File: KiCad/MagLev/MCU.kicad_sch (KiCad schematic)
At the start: 70 parts, among them J2 Programming header, J4 USB_B_Micro, Q1 ZX5T851GTA, Q16 TEMT7000X01, U6 ATmega328P-A, U8 FT232RL, U9 LM1117MP-5.0, Y3 J49SMH-16MHz

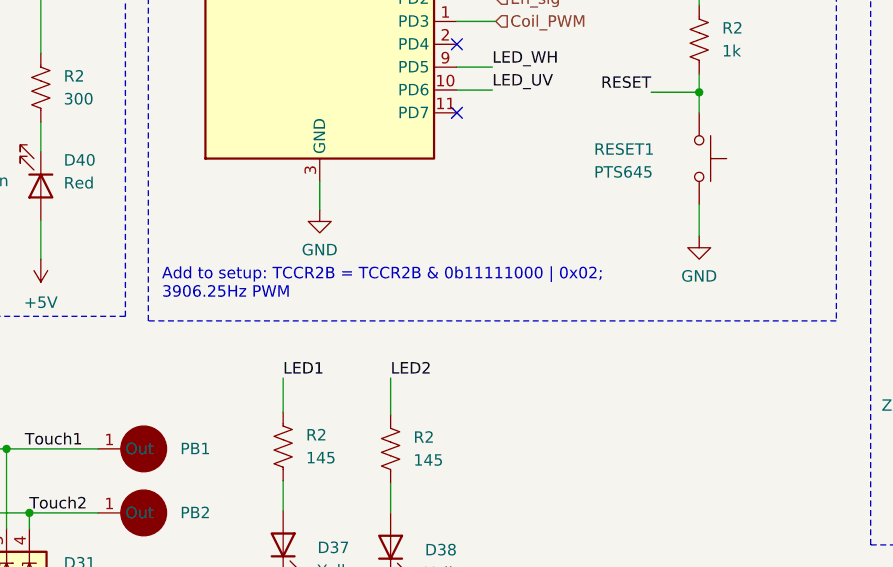
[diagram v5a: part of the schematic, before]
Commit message: Remove silkscreen components from back layer. Cleanup schematic and pcb.
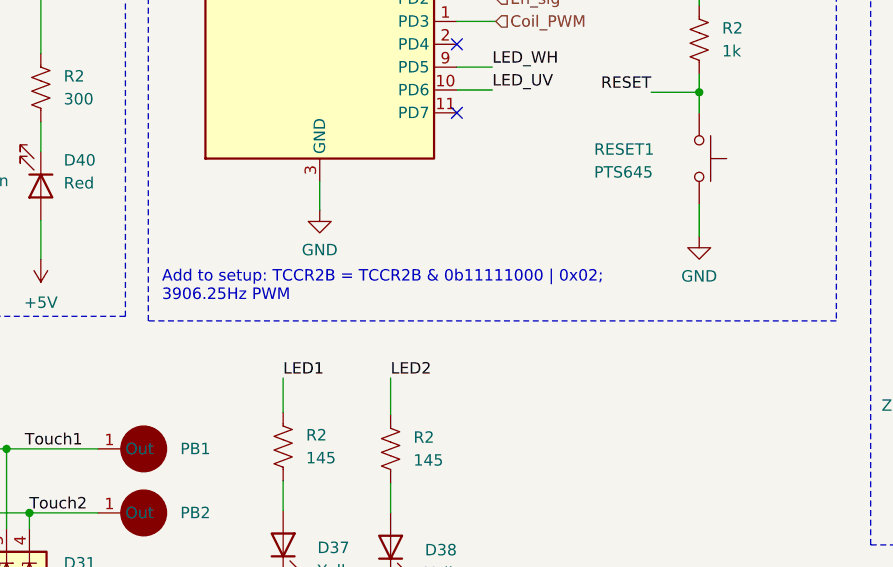
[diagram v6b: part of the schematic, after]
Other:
- company: (none) -> Kevin Dueck
- title: (none) -> MCU Implementation
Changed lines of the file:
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@@
 (kicad_sch (version 20230121) (generator eeschema)
   (paper "A4")
+  (title_block
+    (title "MCU Implementation")
+    (date "2023-08-12")
+    (rev "V1.0")
+    (company "Kevin Dueck")
+  )
   (junction (at 91.694 65.532) (diameter 0) (color 0 0 0 0)
   )
@@
   )
   (text "Add to setup: TCCR2B = TCCR2B & 0b11111000 | 0x02;\n3906.25Hz PWM"
-    (at 141.732 135.636 0)
+    (at 141.732 135.89 0)
     (effects (font (size 1.27 1.27)) (justify left bottom) (href "https://forum.arduino.cc/t/varying-the-pwm-frequency-for-timer-0-or-timer-2/16679/5"))
   )
@@
       (effects (font (size 1.27 1.27)) hide)
     )
-    (pin "2")
-    (pin "1")
-    (instances
-      (project "MagLev"
+    (pin "1")
+    (pin "2")
+    (instances
+      (project "MagLev"

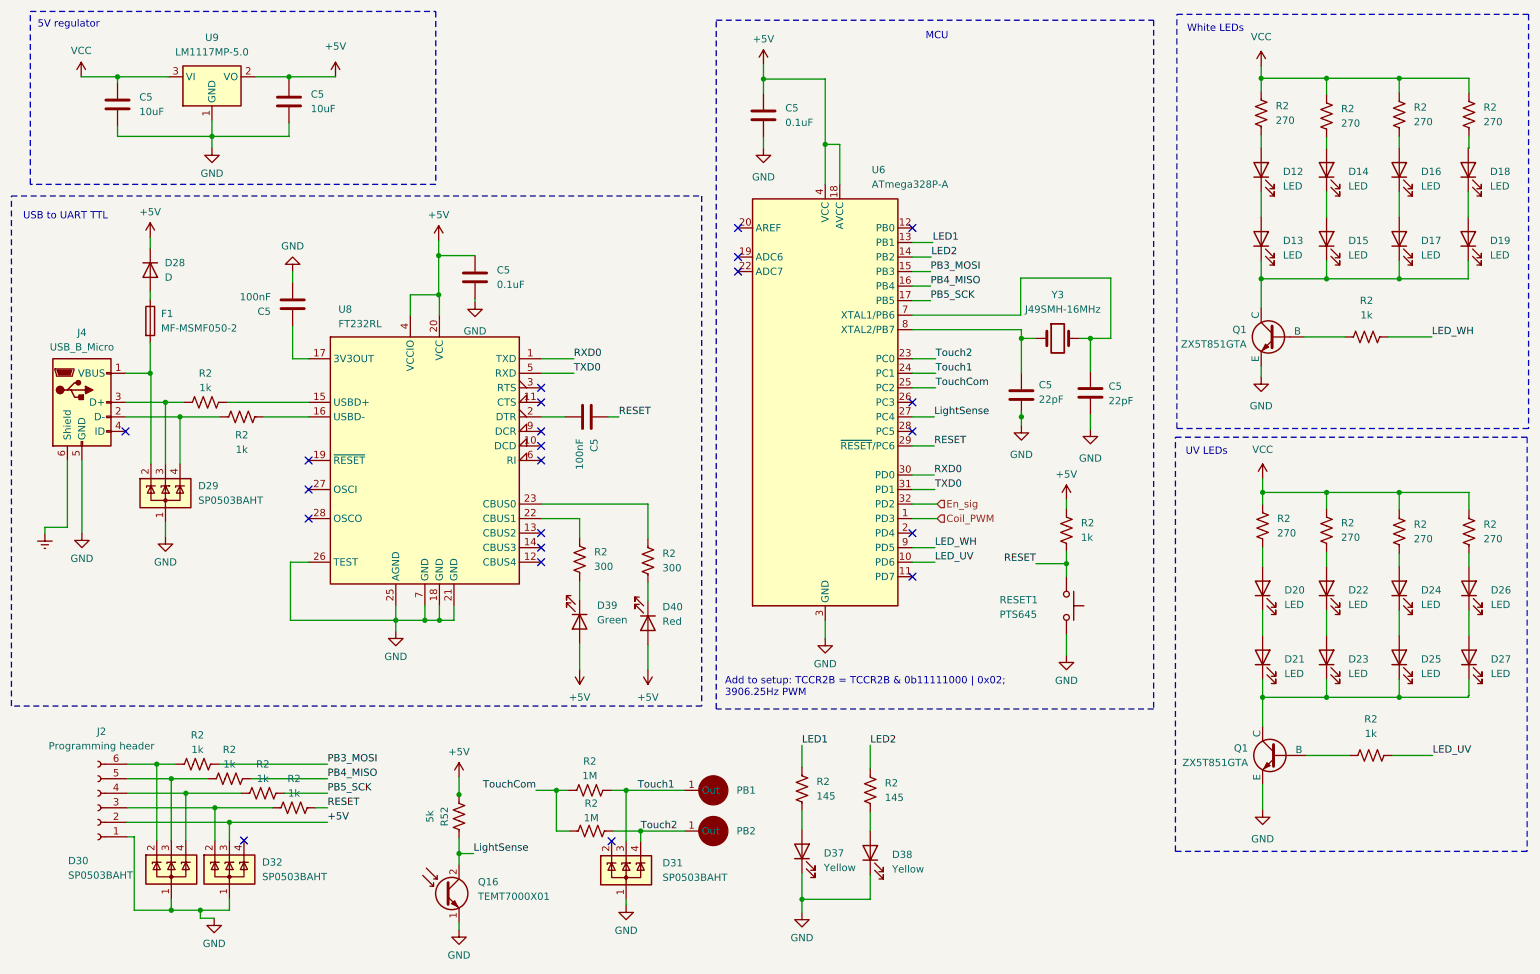
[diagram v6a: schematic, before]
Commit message: Add underglow.
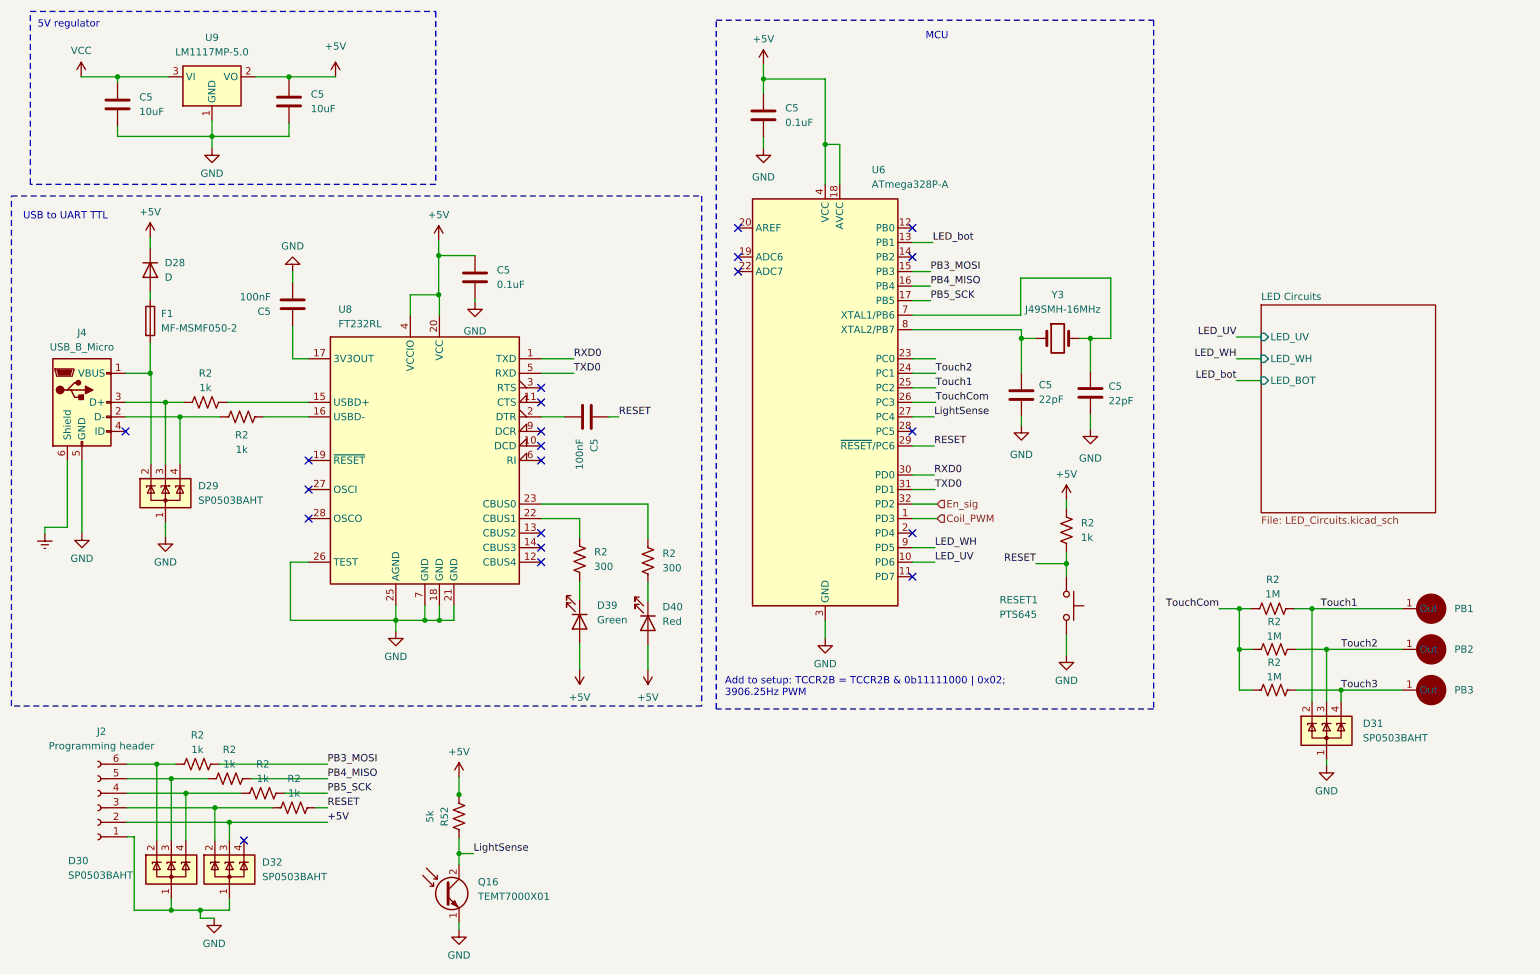
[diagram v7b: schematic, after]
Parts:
- removed D12, D13, D14, D15, D16, D17, D18, D19, D20, D21, D22, D23, D24, D25, D26, D27: LED, LED_SMD:LED_0805_2012Metric_Pad1.15x1.40mm_HandSolder, symbol Device:LED
- removed D37, D38: Yellow, LED_SMD:LED_0805_2012Metric_Pad1.15x1.40mm_HandSolder, symbol Device:LED
- removed Q1 (x2): ZX5T851GTA, Maglev_Footprint_Library:SOT-223-3_TabPin2_BJT, symbol Simulation_SPICE:NPN
- removed R2 (x2): 1k, Resistor_SMD:R_0805_2012Metric_Pad1.20x1.40mm_HandSolder, symbol Device:R_US
- removed R2 (x8): 270, Resistor_SMD:R_0805_2012Metric_Pad1.20x1.40mm_HandSolder, symbol Device:R_US
- removed R2 (x2): 145, Resistor_SMD:R_0805_2012Metric_Pad1.20x1.40mm_HandSolder, symbol Device:R_US
- added PB3: ~, Maglev_Footprint_Library:Capacitive_Touch_Pad, symbol MagLev_Library:Cap_Touch
- added R2: 1M, Resistor_SMD:R_0805_2012Metric_Pad1.20x1.40mm_HandSolder, symbol Device:R_US
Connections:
- net Touch1: now also D31.2 (K), U6.25 (PC2); no longer D31.3 (K), U6.24 (PC1)
- net Touch2: now also D31.3 (K), U6.24 (PC1); no longer D31.4 (K), U6.23 (PC0)
- net TouchCom: now also U6.26 (PC3), R2.2; no longer U6.25 (PC2)
- net LED1 renamed LED_bot
- net LED2: no longer names the net of U6.14 (PB2)
- new net Touch3: D31.4 (K), PB3.1 (Out), R2.1
- no-connect marks 22 -> 21
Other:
- added sheet LED Circuits (LED_Circuits.kicad_sch)
- note removed: "UV LEDs"
- note removed: "White LEDs"
- moved on the sheet: D31, PB1, PB2, R2

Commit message: Update LED PCB reference after adding new LED schematic sheet.
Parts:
- D39: PN (none) -> SML-LXT0805GW-TR; Part SML-LXT0805GW-TR -> (none)
- D40: PN (none) -> SML-LXT0805IW-TR; Part SML-LXT0805IW-TR -> (none)
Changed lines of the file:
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@@
+      (effects (font (size 1.27 1.27)) hide)
+    )
+    (property "JLC Part Number" "" (at 205.613 82.677 0)
       (effects (font (size 1.27 1.27)) hide)
     )
@@
     )
     (property "Datasheet" "~" (at 116.332 111.76 0)
+      (effects (font (size 1.27 1.27)) hide)
+    )
+    (property "JLC Part Number" "" (at 116.332 111.76 0)
       (effects (font (size 1.27 1.27)) hide)
     )
@@
       (effects (font (size 1.27 1.27)) hide)
     )
+    (property "JLC Part Number" "" (at 265.176 139.446 0)
+      (effects (font (size 1.27 1.27)) hide)
+    )
     (pin "1")
     (instances
@@
       (effects (font (size 1.27 1.27)) hide)
     )
+    (property "JLC Part Number" "" (at 246.888 141.732 0)
+      (effects (font (size 1.27 1.27)) hide)
+    )
     (pin "1")
     (pin "2")
@@
       (effects (font (size 1.27 1.27)) hide)
     )
+    (property "JLC Part Number" "" (at 60.96 152.654 0)
+      (effects (font (size 1.27 1.27)) hide)
+    )
     (pin "1")
     (pin "2")
@@
     )
     (property "Datasheet" "https://www.ftdichip.com/Support/Documents/DataSheets/ICs/DS_FT232R.pdf" (at 89.281 94.488 0)
+      (effects (font (size 1.27 1.27)) hide)
+    )
+    (property "JLC Part Number" "" (at 89.281 94.488 0)
       (effects (font (size 1.27 1.27)) hide)
     )
@@
       (effects (font (size 1.27 1.27)) hide)
     )
+    (property "JLC Part Number" "" (at 201.422 119.888 0)
+      (effects (font (size 1.27 1.27)) hide)
+    )
     (pin "1")
     (pin "2")
@@
     )
     (property "Datasheet" "http://www.ti.com/lit/ds/symlink/lm1117.pdf" (at 52.07 27.432 0)
+      (effects (font (size 1.27 1.27)) hide)
+    )
+    (property "JLC Part Number" "" (at 52.07 27.432 0)
       (effects (font (size 1.27 1.27)) hide)
     )
@@
       (effects (font (size 1.27 1.27)) hide)
     )
+    (property "JLC Part Number" "" (at 55.118 165.989 0)
+      (effects (font (size 1.27 1.27)) hide)
+    )
     (pin "1")
     (pin "2")
@@
       (effects (font (size 1.27 1.27)) hide)
     )
+    (property "JLC Part Number" "" (at 43.942 100.203 0)
+      (effects (font (size 1.27 1.27)) hide)
+    )
     (pin "1")
     (pin "2")
@@
       (effects (font (size 1.27 1.27)) hide)
     )
+    (property "JLC Part Number" "" (at 65.532 31.75 0)
+      (effects (font (size 1.27 1.27)) hide)
+    )
     (pin "1")
     (pin "2")
@@
       (effects (font (size 1.27 1.27)) hide)
     )
+    (property "JLC Part Number" "" (at 50.927 84.328 0)
+      (effects (font (size 1.27 1.27)) hide)
+    )
     (pin "1")
     (pin "2")
@@
     )
     (property "Datasheet" "~" (at 148.463 34.163 0)
+      (effects (font (size 1.27 1.27)) hide)
+    )
+    (property "JLC Part Number" "" (at 148.463 34.163 0)
       (effects (font (size 1.27 1.27)) hide)
     )
@@
       (effects (font (size 1.27 1.27)) hide)
     )
+    (property "JLC Part Number" "" (at 265.176 132.334 0)
+      (effects (font (size 1.27 1.27)) hide)
+    )
     (pin "1")
     (instances
@@
       (effects (font (size 1.27 1.27)) hide)
     )
+    (property "JLC Part Number" "" (at 35.56 32.258 0)
+      (effects (font (size 1.27 1.27)) hide)
+    )
     (pin "1")
     (pin "2")
@@
     )
     (property "Datasheet" "~" (at 33.147 85.598 0)
+      (effects (font (size 1.27 1.27)) hide)
+    )
+    (property "JLC Part Number" "" (at 29.337 84.328 0)
       (effects (font (size 1.27 1.27)) hide)
     )
@@
       (effects (font (size 1.27 1.27)) hide)
     )
+    (property "JLC Part Number" "" (at 66.421 155.194 0)
+      (effects (font (size 1.27 1.27)) hide)
+    )
     (pin "1")
     (pin "2")
@@
       (effects (font (size 1.27 1.27)) hide)
     )
+    (property "JLC Part Number" "" (at 95.25 156.718 0)
+      (effects (font (size 1.27 1.27)) hide)
+    )
     (pin "1")
     (pin "2")
@@
       (effects (font (size 1.27 1.27)) hide)
     )
-    (property "Part" "SML-LXT0805GW-TR" (at 116.332 122.682 90)
+    (property "Part" "" (at 116.332 122.682 90)
+      (effects (font (size 1.27 1.27)) hide)
+    )
+    (property "JLC Part Number" "" (at 116.332 122.682 0)
+      (effects (font (size 1.27 1.27)) hide)
+    )
+    (property "PN" "SML-LXT0805GW-TR" (at 116.332 122.682 0)
       (effects (font (size 1.27 1.27)) hide)
     )
@@
       (effects (font (size 1.27 1.27)) hide)
     )
+    (property "JLC Part Number" "" (at 201.422 106.68 0)
+      (effects (font (size 1.27 1.27)) hide)
+    )
     (pin "1")
     (pin "2")
@@
       (effects (font (size 1.27 1.27)) hide)
     )
+    (property "JLC Part Number" "" (at 193.548 83.058 0)
+      (effects (font (size 1.27 1.27)) hide)
+    )
     (pin "1")
     (pin "2")
@@
       (effects (font (size 1.27 1.27)) hide)
     )
+    (property "JLC Part Number" "" (at 237.744 134.62 0)
+      (effects (font (size 1.27 1.27)) hide)
+    )
     (pin "1")
     (pin "2")
@@
       (effects (font (size 1.27 1.27)) hide)
     )
+    (property "JLC Part Number" "" (at 49.53 147.574 0)
+      (effects (font (size 1.27 1.27)) hide)
+    )
     (pin "1")
     (pin "2")
@@
     )
     (property "Datasheet" "~" (at 92.71 170.18 0)
+      (effects (font (size 1.27 1.27)) hide)
+    )
+    (property "JLC Part Number" "" (at 92.71 170.18 0)
       (effects (font (size 1.27 1.27)) hide)
     )
@@
       (effects (font (size 1.27 1.27)) hide)
     )
+    (property "JLC Part Number" "" (at 44.958 165.989 0)
+      (effects (font (size 1.27 1.27)) hide)
+    )
     (pin "1")
     (pin "2")
@@
       (effects (font (size 1.27 1.27)) hide)
     )
+    (property "JLC Part Number" "" (at 237.49 120.396 0)
+      (effects (font (size 1.27 1.27)) hide)
+    )
     (pin "1")
     (pin "2")
@@
     )
     (property "Datasheet" "~" (at 41.275 70.104 0)
+      (effects (font (size 1.27 1.27)) hide)
+    )
+    (property "JLC Part Number" "" (at 41.275 70.104 0)
       (effects (font (size 1.27 1.27)) hide)
     )
@@
       (effects (font (size 1.27 1.27)) hide)
     )
+    (property "JLC Part Number" "" (at 265.176 125.222 0)
+      (effects (font (size 1.27 1.27)) hide)
+    )
     (pin "1")
     (instances
@@
     )
     (property "Datasheet" "~" (at 32.131 155.194 0)
+      (effects (font (size 1.27 1.27)) hide)
+    )
+    (property "JLC Part Number" "" (at 32.131 155.194 0)
       (effects (font (size 1.27 1.27)) hide)
     )
@@
       (effects (font (size 1.27 1.27)) hide)
     )
+    (property "JLC Part Number" "" (at 98.044 62.484 0)
+      (effects (font (size 1.27 1.27)) hide)
+    )
     (pin "1")
     (pin "2")
@@
       (effects (font (size 1.27 1.27)) hide)
     )
+    (property "JLC Part Number" "" (at 57.277 86.868 0)
+      (effects (font (size 1.27 1.27)) hide)
+    )
     (pin "1")
     (pin "2")
@@
       (effects (font (size 1.27 1.27)) hide)
     )
+    (property "JLC Part Number" "" (at 66.167 67.183 0)
+      (effects (font (size 1.27 1.27)) hide)
+    )
     (pin "1")
     (pin "2")
@@
       (effects (font (size 1.27 1.27)) hide)
     )
+    (property "JLC Part Number" "" (at 117.602 86.868 0)
+      (effects (font (size 1.27 1.27)) hide)
+    )
     (pin "1")
     (pin "2")
@@
     )
     (property "Datasheet" "~" (at 199.898 73.152 0)
+      (effects (font (size 1.27 1.27)) hide)
+    )
+    (property "JLC Part Number" "" (at 199.898 73.152 0)
       (effects (font (size 1.27 1.27)) hide)
     )
@@
     )
     (property "Datasheet" "http://ww1.microchip.com/downloads/en/DeviceDoc/ATmega328_P%20AVR%20MCU%20with%20picoPower%20Technology%20Data%20Sheet%2040001984A.pdf" (at 159.258 84.328 0)
+      (effects (font (size 1.27 1.27)) hide)
+    )
+    (property "JLC Part Number" "" (at 159.258 84.328 0)
       (effects (font (size 1.27 1.27)) hide)
     )
@@
       (effects (font (size 1.27 1.27)) hide)
     )
+    (property "JLC Part Number" "" (at 237.744 127.508 0)
+      (effects (font (size 1.27 1.27)) hide)
+    )
     (pin "1")
     (pin "2")
@@
       (effects (font (size 1.27 1.27)) hide)
     )
+    (property "JLC Part Number" "" (at 128.27 112.014 0)
+      (effects (font (size 1.27 1.27)) hide)
+    )
     (pin "1")
     (pin "2")
@@
       (effects (font (size 1.27 1.27)) hide)
     )
-    (property "Part" "SML-LXT0805IW-TR" (at 128.27 122.936 90)
+    (property "Part" "" (at 128.27 122.936 90)
+      (effects (font (size 1.27 1.27)) hide)
+    )
+    (property "JLC Part Number" "" (at 128.27 122.936 0)
+      (effects (font (size 1.27 1.27)) hide)
+    )
+    (property "PN" "SML-LXT0805IW-TR" (at 128.27 122.936 0)
       (effects (font (size 1.27 1.27)) hide)
     )
@@
       (effects (font (size 1.27 1.27)) hide)
     )
+    (property "JLC Part Number" "" (at 55.118 150.114 0)
+      (effects (font (size 1.27 1.27)) hide)
+    )
     (pin "1")
     (pin "2")
@@
       (effects (font (size 1.27 1.27)) hide)
     )
+    (property "JLC Part Number" "" (at 41.275 61.214 0)
+      (effects (font (size 1.27 1.27)) hide)
+    )
